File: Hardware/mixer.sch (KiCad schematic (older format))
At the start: 6 parts, among them U5 TL072

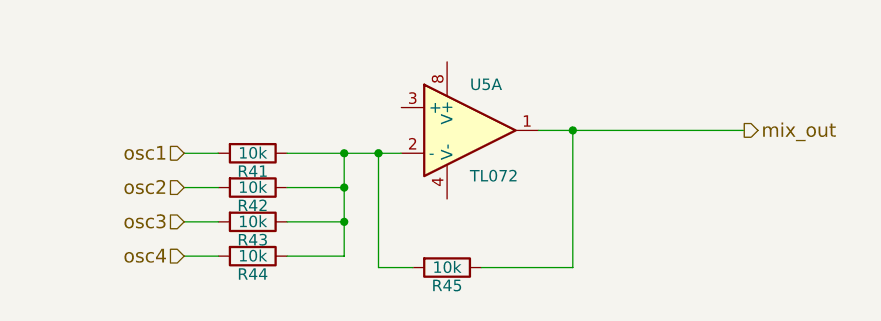
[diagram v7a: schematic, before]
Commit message: add VREF to all single supply op amps
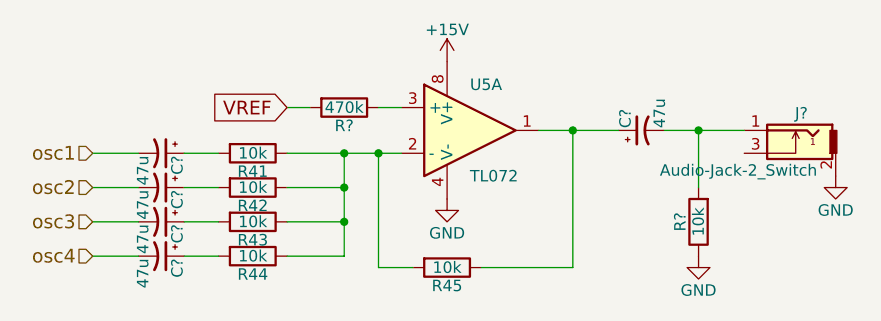
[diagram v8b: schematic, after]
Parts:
- added C? (x5): 47u, symbol CP1_Small
- added J?: Audio-Jack-2_Switch, symbol Audio-Jack-2_Switch
- added R?: 10k, symbol R
- added R?: 470k, symbol R
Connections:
- net osc1: now also C?.2; no longer R41.2
- net osc2: now also C?.2; no longer R42.2
- net osc3: now also C?.2; no longer R43.2
- net osc4: now also C?.2; no longer R44.2
- net at U5.3 (+): now also R?.1
- net GND: now reaches U5.4 (V-)
- net GND: now also J?.2, R?.1
- net +15V: now reaches U5.8 (V+)
- net mix_out: no longer names the net of R45.1, U5.1
- net mix_out: now also C?.1
- new net: C?.1, R41.2
- new net: C?.1, R42.2
- new net: C?.1, R43.2
- new net: C?.1, R44.2
- new net: C?.2, J?.1, R?.2
- new net VREF: R?.2
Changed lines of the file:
@@
 $Descr A4 11693 8268
 encoding utf-8
-Sheet 5 8
+Sheet 5 7
 Title ""
 Date ""
@@
 Comment4 ""
 $EndDescr
-Text HLabel 4900 3600 0    60   Input ~ 0
+Text HLabel 4500 3600 0    60   Input ~ 0
 osc1
-Text HLabel 4900 3750 0    60   Input ~ 0
+Text HLabel 4500 3750 0    60   Input ~ 0
 osc2
-Text HLabel 4900 3900 0    60   Input ~ 0
+Text HLabel 4500 3900 0    60   Input ~ 0
 osc3
-Text HLabel 4900 4050 0    60   Input ~ 0
+Text HLabel 4500 4050 0    60   Input ~ 0
 osc4
 $Comp
@@
 $EndComp
 Wire Wire Line
-	4900 3600 5050 3600
-Wire Wire Line
-	4900 3750 5050 3750
-Wire Wire Line
-	4900 3900 5050 3900
-Wire Wire Line
-	4900 4050 5050 4050
+	4500 3600 4700 3600
+Wire Wire Line
+	4500 3750 4700 3750
+Wire Wire Line
+	4500 3900 4700 3900
+Wire Wire Line
+	4500 4050 4700 4050
 $Comp
 L TL072 U5
@@
 	6600 4100 6600 3500
 Wire Wire Line
-	6450 3500 7350 3500
-Wire Wire Line
 	5900 4100 5750 4100
 Wire Wire Line
-	5750 4100 5750 3600
+	5750 3600 5750 4100
 Wire Wire Line
 	5350 3600 5850 3600
 Connection ~ 5750 3600
 Wire Wire Line
-	5350 4050 5600 4050
+	5600 4050 5350 4050
 Wire Wire Line
 	5350 3750 5600 3750
@@
 Connection ~ 5600 3600
 Wire Wire Line
-	5350 3900 5600 3900
+	5600 3900 5350 3900
 Connection ~ 5600 3900
 Wire Wire Line
-	5600 4050 5600 3600
-Text HLabel 7350 3500 2    60   Output ~ 0
-mix_out
+	5600 3600 5600 4050
 Connection ~ 6600 3500
+$Comp
+L Audio-Jack-2_Switch J?
+U 1 1 5C394BFE
+P 7550 3600
+F 0 "J?" H 7500 3775 50  0000 C CNN
+F 1 "Audio-Jack-2_Switch" H 7775 3525 50  0000 C CNN
+F 2 "" H 7800 3700 50  0001 C CNN
+F 3 "" H 7800 3700 50  0001 C CNN
+	1    7550 3600
+	-1   0    0    -1
+$EndComp
+$Comp
+L GND #PWR?
+U 1 1 5C394C8E
+P 7750 3700
+F 0 "#PWR?" H 7750 3450 50  0001 C CNN
+F 1 "GND" H 7750 3550 50  0000 C CNN
+F 2 "" H 7750 3700 50  0001 C CNN
+F 3 "" H 7750 3700 50  0001 C CNN
+	1    7750 3700
+	1    0    0    -1
+$EndComp
+$Comp
+L CP1_Small C?
+U 1 1 5C396119
+P 4800 3600
+F 0 "C?" H 4810 3670 50  0000 L CNN
+F 1 "47u" H 4810 3520 50  0000 L CNN
+F 2 "" H 4800 3600 50  0001 C CNN
+F 3 "" H 4800 3600 50  0001 C CNN
+	1    4800 3600
+	0    1    1    0
+$EndComp
+$Comp
+L CP1_Small C?
+U 1 1 5C396261
+P 4800 3750
+F 0 "C?" H 4810 3820 50  0000 L CNN
+F 1 "47u" H 4810 3670 50  0000 L CNN
+F 2 "" H 4800 3750 50  0001 C CNN
+F 3 "" H 4800 3750 50  0001 C CNN
+	1    4800 3750
+	0    1    1    0
+$EndComp
+$Comp
+L CP1_Small C?
+U 1 1 5C39628E
+P 4800 3900
+F 0 "C?" H 4810 3970 50  0000 L CNN
+F 1 "47u" H 4810 3820 50  0000 L CNN
+F 2 "" H 4800 3900 50  0001 C CNN
+F 3 "" H 4800 3900 50  0001 C CNN
+	1    4800 3900
+	0    1    1    0
+$EndComp
+$Comp
+L CP1_Small C?
+U 1 1 5C3962BE
+P 4800 4050
+F 0 "C?" H 4810 4120 50  0000 L CNN
+F 1 "47u" H 4810 3970 50  0000 L CNN
+F 2 "" H 4800 4050 50  0001 C CNN
+F 3 "" H 4800 4050 50  0001 C CNN
+	1    4800 4050
+	0    1    1    0
+$EndComp
+Wire Wire Line
+	5050 4050 4900 4050
+Wire Wire Line
+	4900 3900 5050 3900
+Wire Wire Line
+	5050 3750 4900 3750
+Wire Wire Line
+	4900 3600 5050 3600
+$Comp
+L GND #PWR?
+U 1 1 5C396479
+P 6050 3800
+F 0 "#PWR?" H 6050 3550 50  0001 C CNN
+F 1 "GND" H 6050 3650 50  0000 C CNN
+F 2 "" H 6050 3800 50  0001 C CNN
+F 3 "" H 6050 3800 50  0001 C CNN
+	1    6050 3800
+	1    0    0    -1
+$EndComp
+$Comp
+L CP1_Small C?
+U 1 1 5C3964A5
+P 6900 3500
+F 0 "C?" H 6910 3570 50  0000 L CNN
+F 1 "47u" H 6910 3420 50  0000 L CNN
+F 2 "" H 6900 3500 50  0001 C CNN
+F 3 "" H 6900 3500 50  0001 C CNN
+	1    6900 3500
+	0    -1   -1   0
+$EndComp
+Wire Wire Line
+	6450 3500 6800 3500
+Wire Wire Line
+	7000 3500 7350 3500
+$Comp
+L R R?
+U 1 1 5C3965C9
+P 7150 3900
+F 0 "R?" V 7230 3900 50  0000 C CNN
+F 1 "10k" V 7150 3900 50  0000 C CNN
+F 2 "" V 7080 3900 50  0001 C CNN
+F 3 "" H 7150 3900 50  0001 C CNN
+	1    7150 3900
+	-1   0    0    1
+$EndComp
+Wire Wire Line
+	7150 3750 7150 3500
+Connection ~ 7150 3500
+$Comp
+L GND #PWR?
+U 1 1 5C39665C
+P 7150 4050
+F 0 "#PWR?" H 7150 3800 50  0001 C CNN
+F 1 "GND" H 7150 3900 50  0000 C CNN
+F 2 "" H 7150 4050 50  0001 C CNN
+F 3 "" H 7150 4050 50  0001 C CNN
+	1    7150 4050
+	1    0    0    -1
+$EndComp
+$Comp
+L +15V #PWR?
+U 1 1 5C396690
+P 6050 3200
+F 0 "#PWR?" H 6050 3050 50  0001 C CNN
+F 1 "+15V" H 6050 3340 50  0000 C CNN
+F 2 "" H 6050 3200 50  0001 C CNN
+F 3 "" H 6050 3200 50  0001 C CNN
+	1    6050 3200
+	1    0    0    -1
+$EndComp
+Text GLabel 5350 3400 0    60   Input ~ 0
+VREF
+$Comp
+L R R?
+U 1 1 5C39670B
+P 5600 3400
+F 0 "R?" V 5680 3400 50  0000 C CNN
+F 1 "470k" V 5600 3400 50  0000 C CNN
+F 2 "" V 5530 3400 50  0001 C CNN
+F 3 "" H 5600 3400 50  0001 C CNN
+	1    5600 3400
+	0    1    1    0
+$EndComp
+Wire Wire Line
+	5750 3400 5850 3400
+Wire Wire Line
+	5350 3400 5450 3400
 $EndSCHEMATC
